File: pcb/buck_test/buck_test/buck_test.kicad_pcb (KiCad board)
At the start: 2 copper layers, 141.6 x 88.9 mm, 34 parts, among them U1 MC34063AD, U2 AP3402, U3 Würth 171010502

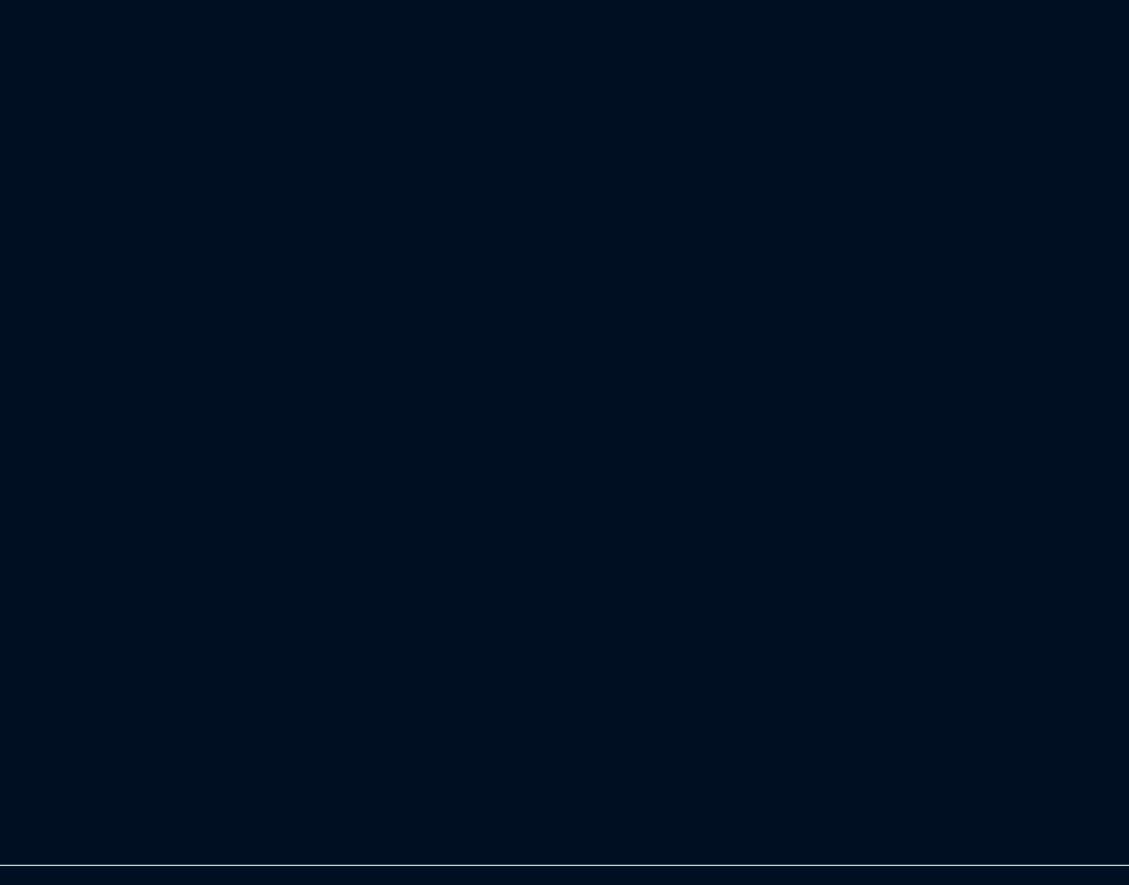
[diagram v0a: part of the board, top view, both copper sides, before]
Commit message: [WIP] Tests to allow mounting BT module coplanar with PCB
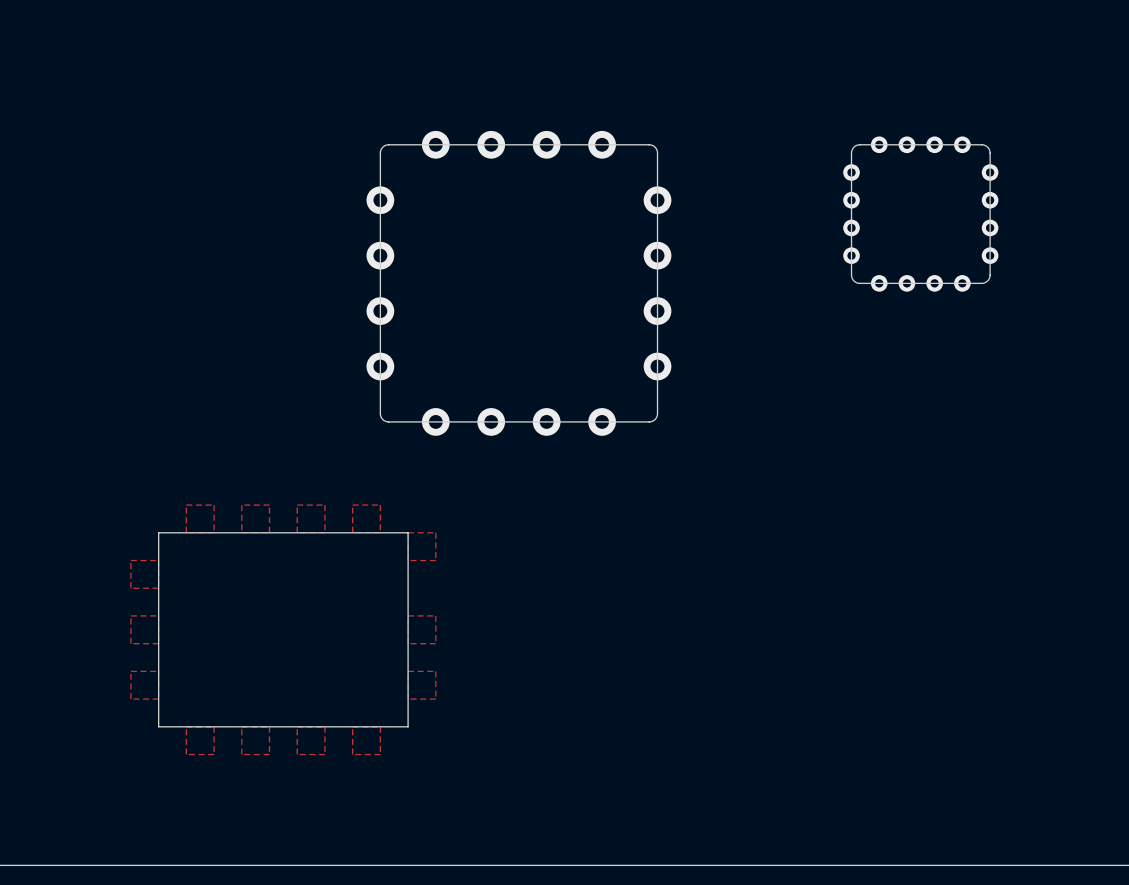
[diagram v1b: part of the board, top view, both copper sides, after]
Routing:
- net (no net): vias 0 -> 32
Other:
- outline, holes or cut-outs redrawn
- board text added: "tests for internal castellation to mount BT module inside a cutout so it doesn't add to the thickness. todo: add footprint to BT module library that has pads fully outside the board outline and possibly includes the cutout. otherwise, pads only, and add cutout on pcb. consider using copper tape under module to act as ground plane"
